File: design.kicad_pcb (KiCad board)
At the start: 2 copper layers, 102.2 x 38.6 mm, 38 parts, among them J1 HRO_TYPE-C-31-M-12, J2 SKEDD:490107670612, J3 Conn_02x03_Odd_Even, SW1 EN, SW2 IO9, SW3 5V/3.3V, SW4 VDD/NC, U1 MCP1700x-330xxTT, U2 TCK108AF,LF, U3 ESP32-C3-WROOM-02-N4, U4 TTP223, U5 MCP1700x-330xxTT

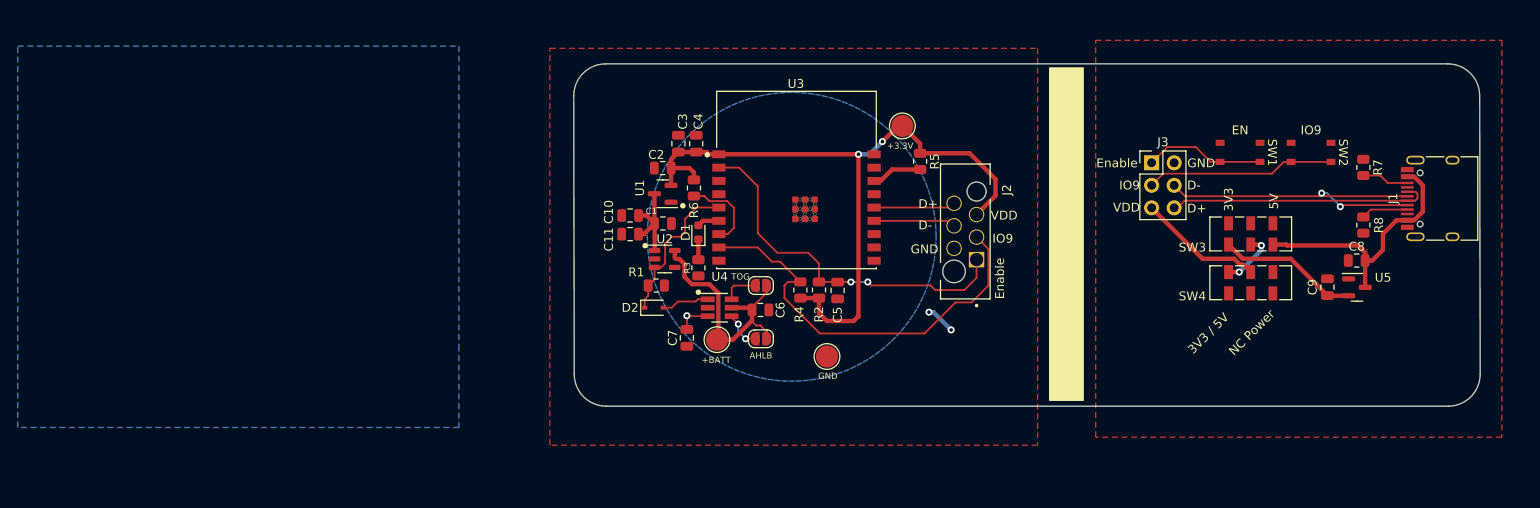
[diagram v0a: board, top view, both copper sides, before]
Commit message: make PCB smaller again
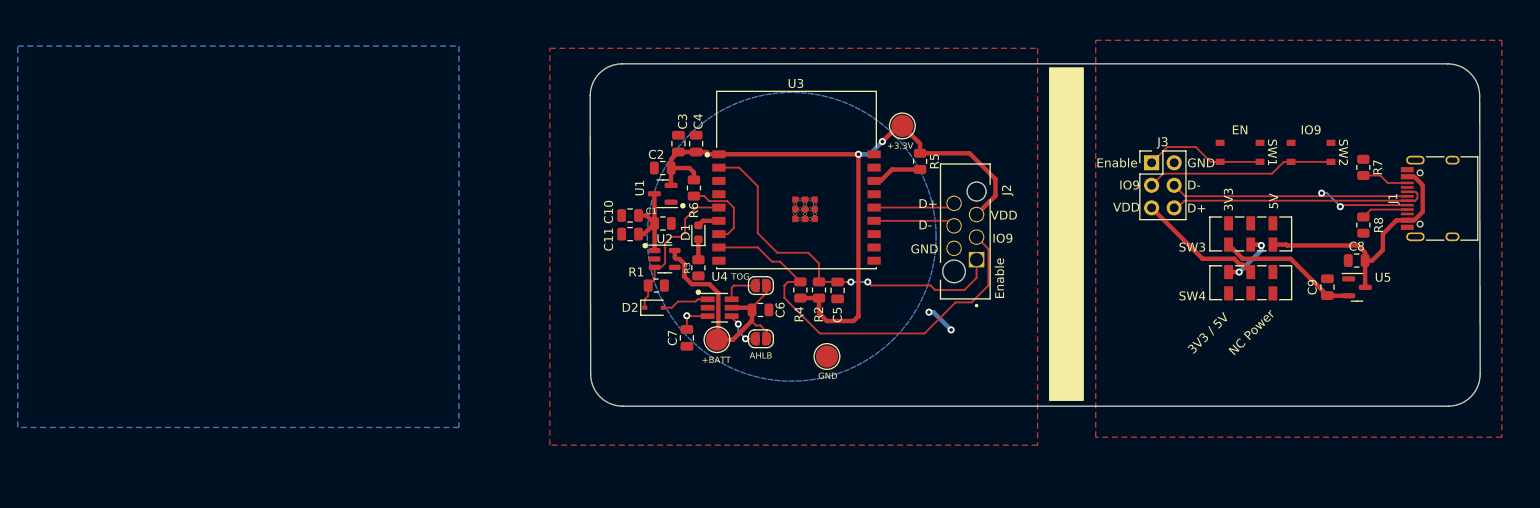
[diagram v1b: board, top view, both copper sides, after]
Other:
- board size 102.2 x 38.6 mm -> 100.4 x 38.6 mm
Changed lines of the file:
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@@
   (gr_circle (center 137.25 96) (end 137.5 96) (layer "F.SilkS") (width 0.12) (fill solid))
   (gr_rect (start 178.6 117.95) (end 182.4 80.45) (layer "F.SilkS") (width 0.12) (fill solid))
-  (gr_arc (start 124.945584 83.6) (mid 126 81.054416) (end 128.545584 80) (layer "Edge.Cuts") (width 0.12))
+  (gr_arc (start 126.8 83.6) (mid 127.854415 81.05441) (end 130.4 80) (layer "Edge.Cuts") (width 0.12))
   (gr_line (start 227.1 83.6) (end 227.154416 115) (layer "Edge.Cuts") (width 0.05))
   (gr_arc (start 223.5 80) (mid 226.045584 81.054416) (end 227.1 83.6) (layer "Edge.Cuts") (width 0.12))
-  (gr_line (start 124.945584 83.6) (end 125 115) (layer "Edge.Cuts") (width 0.05))
-  (gr_arc (start 128.6 118.6) (mid 126.054416 117.545584) (end 125 115) (layer "Edge.Cuts") (width 0.12))
-  (gr_line (start 223.554416 118.6) (end 128.6 118.6) (layer "Edge.Cuts") (width 0.05))
+  (gr_line (start 126.8 83.6) (end 126.854416 115) (layer "Edge.Cuts") (width 0.05))
+  (gr_arc (start 130.454416 118.6) (mid 127.908832 117.545584) (end 126.854416 115) (layer "Edge.Cuts") (width 0.12))
+  (gr_line (start 223.554416 118.6) (end 130.454416 118.6) (layer "Edge.Cuts") (width 0.05))
   (gr_arc (start 227.154416 115) (mid 226.100001 117.54559) (end 223.554416 118.6) (layer "Edge.Cuts") (width 0.12))
-  (gr_line (start 128.545584 80) (end 223.5 80) (layer "Edge.Cuts") (width 0.05))
+  (gr_line (start 130.4 80) (end 223.5 80) (layer "Edge.Cuts") (width 0.05))
   (gr_text "<<project_name>>\n<<ID>>\n<<version>>\n<<date>>\n<<hash>>\n<<website_link>>" (at 150.3 89.6) (layer "B.SilkS")
     (effects (font (size 1 1) (thickness 0.15)) (justify mirror))

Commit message: add copper area on back to balance in production
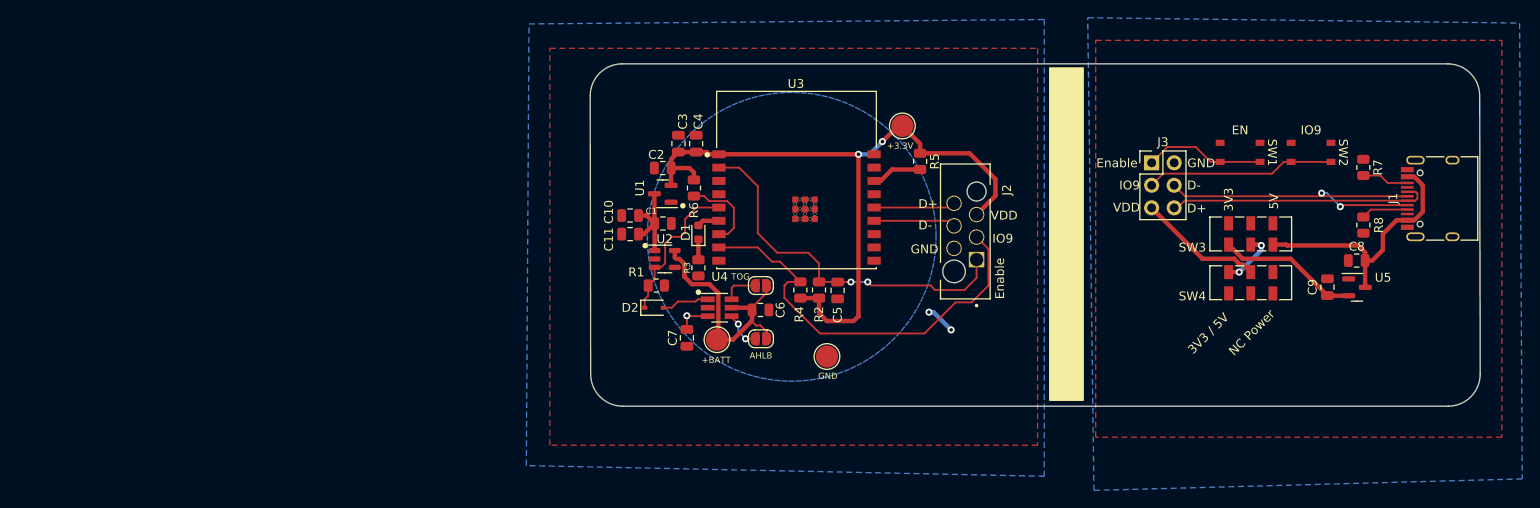
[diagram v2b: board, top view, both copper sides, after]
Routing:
- added copper zone on B.Cu, net GND
- added copper zone on B.Cu, net GND2
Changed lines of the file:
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@@
     (connect_pads (clearance 0.2))
     (min_thickness 0.1) (filled_areas_thickness no)
-    (fill (thermal_gap 0.508) (thermal_bridge_width 0.508))
+    (fill yes (thermal_gap 0.508) (thermal_bridge_width 0.508))
     (polygon
       (pts
@@
     )
   )
-  (zone (net 3) (net_name "touch_point_1") (layer "B.Cu") (hatch edge 0.508)
+  (zone (net 1) (net_name "GND") (layer "B.Cu") (hatch edge 0.508)
+    (priority 1)
     (connect_pads (clearance 0.2))
-    (min_thickness 0.1) (filled_areas_thickness no)
-    (fill yes (mode hatch) (thermal_gap 0.508) (thermal_bridge_width 0.508)
-      (hatch_thickness 0.21) (hatch_gap 5) (hatch_orientation 45)
-      (hatch_smoothing_level 3) (hatch_smoothing_value 0.2)
-      (hatch_border_algorithm hatch_thickness) (hatch_min_hole_area 0.3))
+    (min_thickness 0.254) (filled_areas_thickness no)
+    (fill yes (thermal_gap 0.508) (thermal_bridge_width 0.508))
     (polygon
       (pts
-        (xy 112 111.75)
-        (xy 112 121)
-        (xy 62.25 121)
-        (xy 62.25 78)
-        (xy 112 78)
+        (xy 178 126.5)
+        (xy 119.6 125.3)
+        (xy 119.9 75.5)
+        (xy 178 75)
+      )
+    )
+  )
+  (zone (net 40) (net_name "GND2") (layer "B.Cu") (hatch edge 0.508)
+    (connect_pads (clearance 0.2))
+    (min_thickness 0.254) (filled_areas_thickness no)
+    (fill yes (thermal_gap 0.508) (thermal_bridge_width 0.508))
+    (polygon
+      (pts
+        (xy 231.6 75.4)
+        (xy 231.9 126.8)
+        (xy 183.6 128.1)
+        (xy 182.9 74.8)
       )
     )
   )
   (zone (net 3) (net_name "touch_point_1") (layer "B.Cu") (hatch edge 0.508)
+    (priority 2)
     (connect_pads (clearance 0.2))
     (min_thickness 0.254) (filled_areas_thickness no)

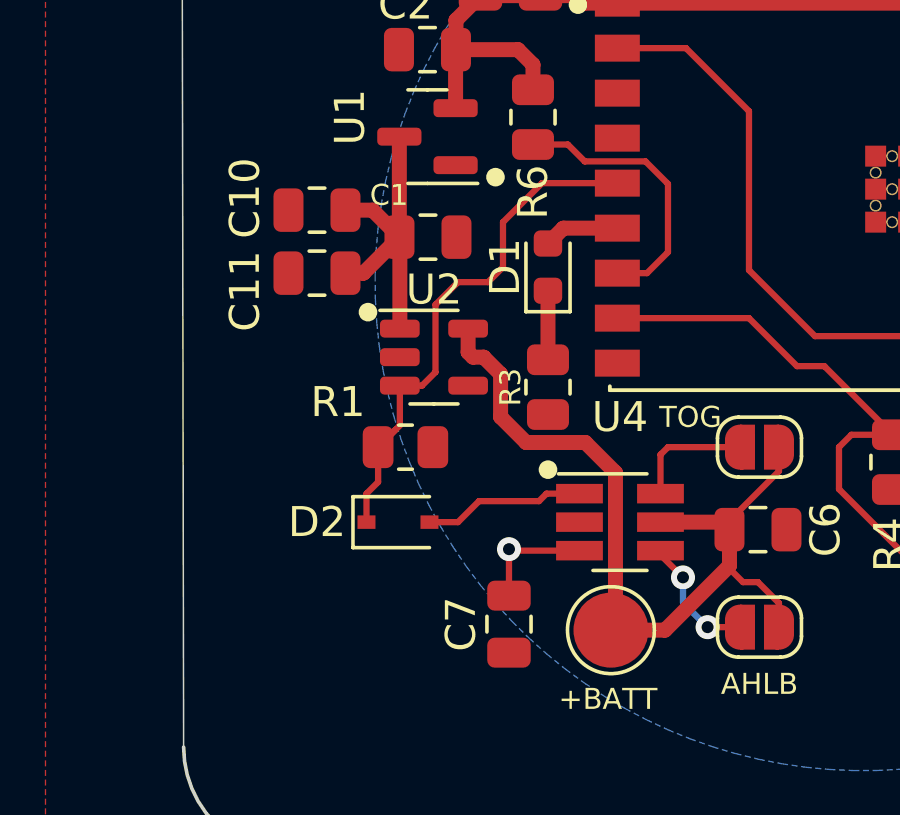
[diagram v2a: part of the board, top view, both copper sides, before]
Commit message: Add second Diode to Touch input
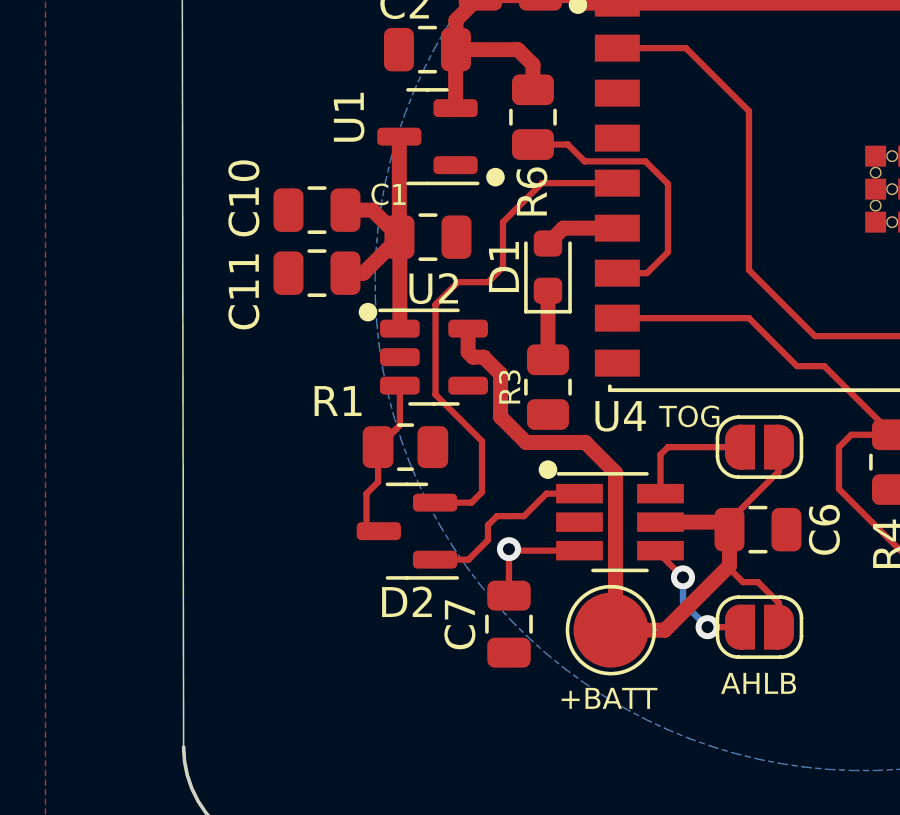
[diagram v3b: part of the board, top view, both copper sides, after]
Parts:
- D2: value D_Small -> BAV70; footprint Diode_SMD:D_SOD-323 -> Package_TO_SOT_SMD:SOT-23
- moved D2 0.42 mm to (134.3, 107.8), turned to 180 degrees
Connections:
- D2 pad 1: PWR_control -> Touch
- D2 pad 2: Net-(D2-Pad2) -> PWR_control
- R1 pad 1: PWR_control -> Net-(R1-Pad1)
- U2 pad 3: PWR_control -> Net-(R1-Pad1)
- U4 pad 1: Net-(D2-Pad2) -> Touch
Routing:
- net Touch: track 0.00 -> 6.02 mm
- net Net-(R1-Pad1): track 0.00 -> 5.84 mm
- net Net-(D2-Pad2): track 5.39 -> 0.00 mm
- net PWR_control: track 18.1 -> 17.2 mm
